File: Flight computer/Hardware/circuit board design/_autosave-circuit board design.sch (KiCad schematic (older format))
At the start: 0 parts

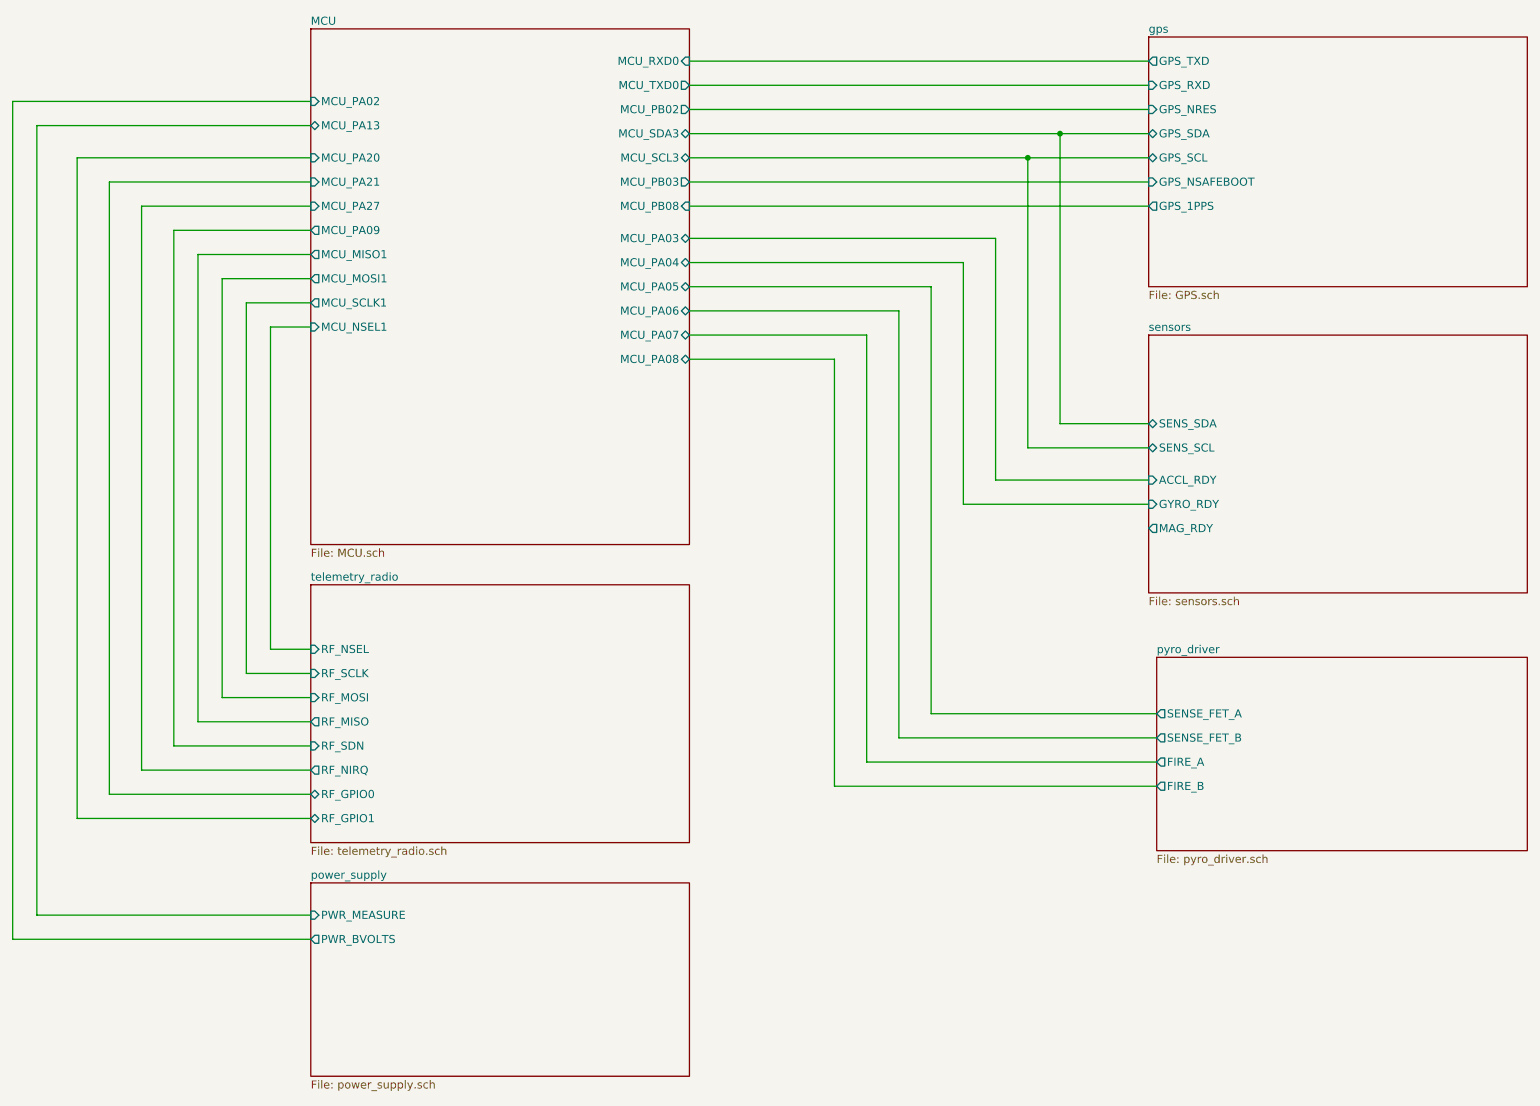
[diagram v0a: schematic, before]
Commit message: put in the IIS2MDC magnetometer
-fixed the error  spi connection pins for Flash chip
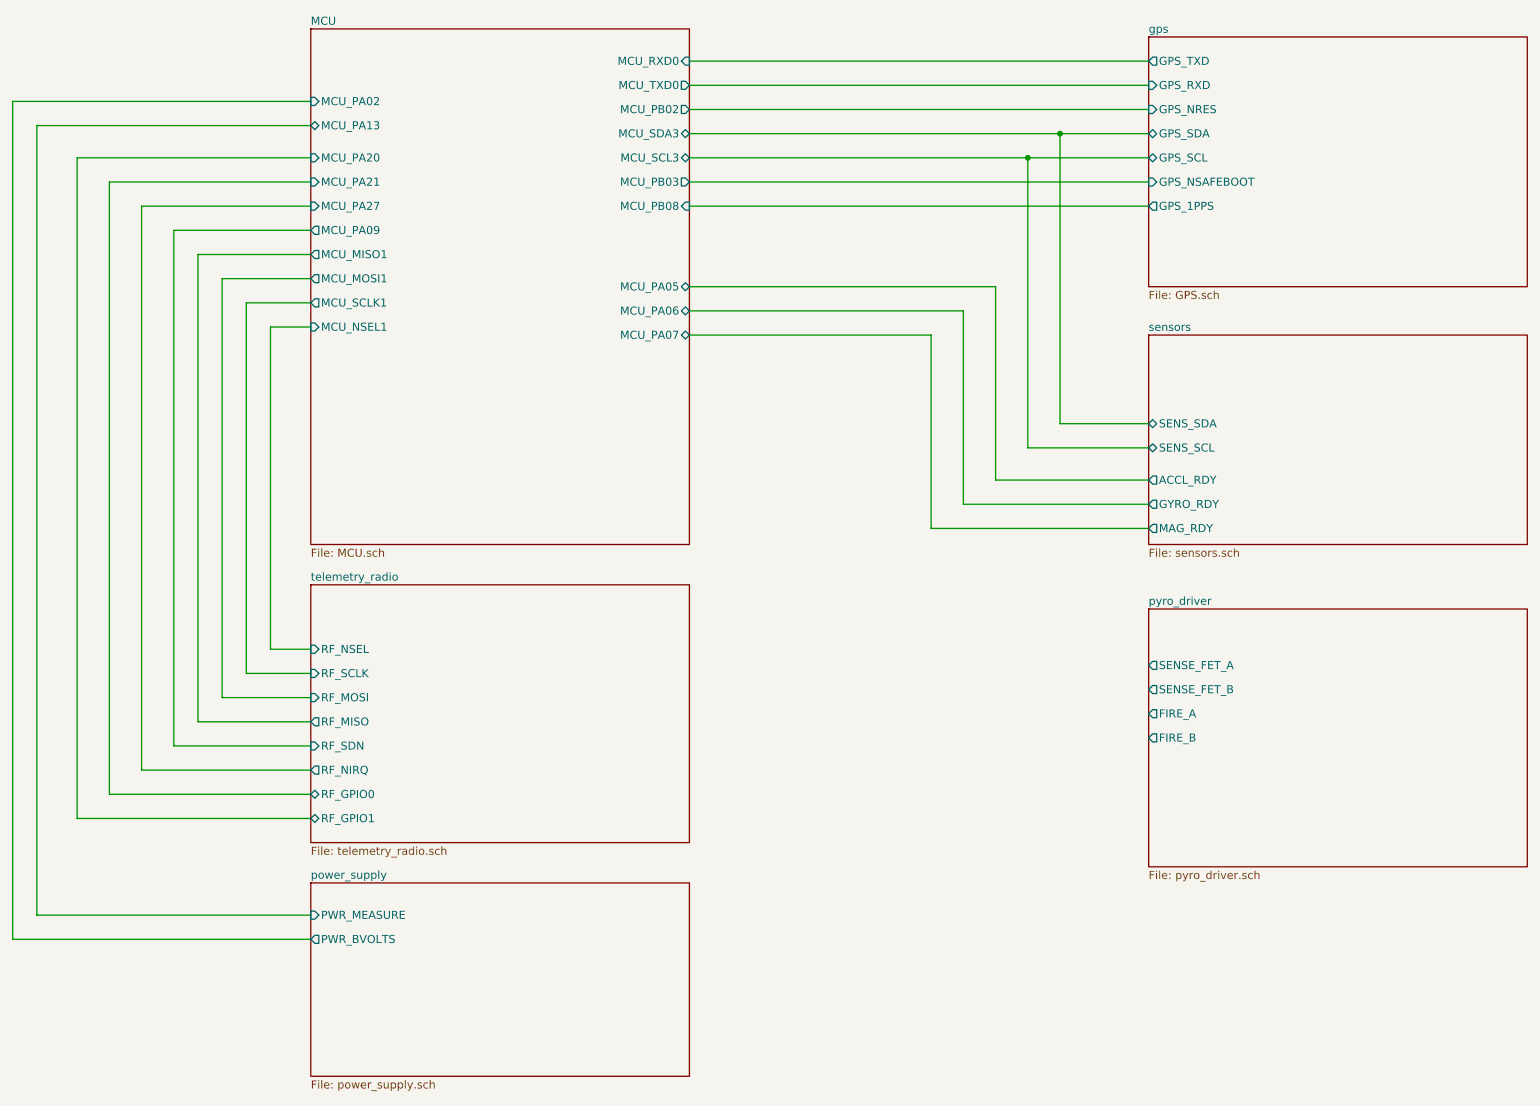
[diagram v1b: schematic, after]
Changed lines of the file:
@@
 $EndDescr
 $Sheet
-S 7900 3000 2350 1600
+S 7900 3000 2350 1300
 U 5D5B1586
 F0 "sensors" 50
@@
 F2 "SENS_SDA" B L 7900 3550 50
 F3 "SENS_SCL" B L 7900 3700 50
-F4 "ACCL_RDY" I L 7900 3900 50
-F5 "GYRO_RDY" I L 7900 4050 50
-F6 "MAG_RDY" O L 7900 4200 50
+F4 "MAG_RDY" O L 7900 4200 50
+F5 "ACCL_RDY" O L 7900 3900 50
+F6 "GYRO_RDY" O L 7900 4050 50
 $EndSheet
 $Sheet
@@
 	7150 1900 7900 1900
 $Sheet
-S 7950 5000 2300 1200
+S 7900 4700 2350 1600
 U 5D6468D5
 F0 "pyro_driver" 50
 F1 "pyro_driver.sch" 50
-F2 "SENSE_FET_A" O L 7950 5350 50
-F3 "FIRE_A" O L 7950 5650 50
-F4 "SENSE_FET_B" O L 7950 5500 50
-F5 "FIRE_B" O L 7950 5800 50
+F2 "SENSE_FET_A" O L 7900 5050 50
+F3 "FIRE_A" O L 7900 5350 50
+F4 "SENSE_FET_B" O L 7900 5200 50
+F5 "FIRE_B" O L 7900 5500 50
 $EndSheet
 Wire Wire Line
 	7900 3900 6950 3900
-Wire Wire Line
-	6950 3900 6950 2400
 $Sheet
 S 2700 6400 2350 1200
@@
 	7900 4050 6750 4050
 Wire Wire Line
-	6750 4050 6750 2550
-Wire Wire Line
-	5950 5800 7950 5800
-Wire Wire Line
-	6150 5650 6150 3000
-Wire Wire Line
-	6350 2850 6350 5500
-Wire Wire Line
-	6550 2700 6550 5350
-Wire Wire Line
-	5950 3150 5950 5800
-Wire Wire Line
-	6550 5350 7950 5350
-Wire Wire Line
-	6350 5500 7950 5500
-Wire Wire Line
-	7950 5650 6150 5650
-Wire Wire Line
 	1650 2200 2700 2200
 Wire Wire Line
@@
 	1850 2350 2700 2350
 Wire Wire Line
-	6750 2550 5050 2550
+	6750 2850 5050 2850
 Wire Wire Line
-	6950 2400 5050 2400
+	6950 2700 5050 2700
 Wire Wire Line
 	2700 1550 850  1550
@@
 Wire Wire Line
 	2150 2650 2700 2650
-Wire Wire Line
-	5050 3150 5950 3150
-Wire Wire Line
-	5050 2700 6550 2700
-Wire Wire Line
-	5050 2850 6350 2850
-Wire Wire Line
-	6150 3000 5050 3000
 $Sheet
 S 2700 1100 2350 3200
@@
 F9 "MCU_RXD0" I R 5050 1300 50
 F10 "MCU_PA02" I L 2700 1550 50
-F11 "MCU_PA03" B R 5050 2400 50
-F12 "MCU_PA04" B R 5050 2550 50
-F13 "MCU_PA05" B R 5050 2700 50
-F14 "MCU_PA06" B R 5050 2850 50
-F15 "MCU_PA07" B R 5050 3000 50
-F16 "MCU_PA08" B R 5050 3150 50
-F17 "MCU_PA09" O L 2700 2350 50
-F18 "MCU_PA13" B L 2700 1700 50
-F19 "MCU_PB03" O R 5050 2050 50
-F20 "MCU_PB02" O R 5050 1600 50
-F21 "MCU_PB08" I R 5050 2200 50
-F22 "MCU_PA20" I L 2700 1900 50
-F23 "MCU_PA21" I L 2700 2050 50
-F24 "MCU_PA27" I L 2700 2200 50
+F11 "MCU_PA05" B R 5050 2700 50
+F12 "MCU_PA06" B R 5050 2850 50
+F13 "MCU_PA07" B R 5050 3000 50
+F14 "MCU_PA09" O L 2700 2350 50
+F15 "MCU_PA13" B L 2700 1700 50
+F16 "MCU_PB03" O R 5050 2050 50
+F17 "MCU_PB02" O R 5050 1600 50
+F18 "MCU_PB08" I R 5050 2200 50
+F19 "MCU_PA20" I L 2700 1900 50
+F20 "MCU_PA21" I L 2700 2050 50
+F21 "MCU_PA27" I L 2700 2200 50
 $EndSheet
+Wire Wire Line
+	5050 3000 6550 3000
+Wire Wire Line
+	6550 3000 6550 4200
+Wire Wire Line
+	6750 4050 6750 2850
+Wire Wire Line
+	6950 3900 6950 2700
+Wire Wire Line
+	6550 4200 7900 4200
 $EndSCHEMATC
